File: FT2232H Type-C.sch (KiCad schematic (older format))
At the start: 34 parts, among them J1 CONN_01X20, J2 CONN_01X20, J3 USB_TYPE_C, U1 LD1117S33TR, U3 93CxxB, U4 FT2232H, Y1 12Mhz

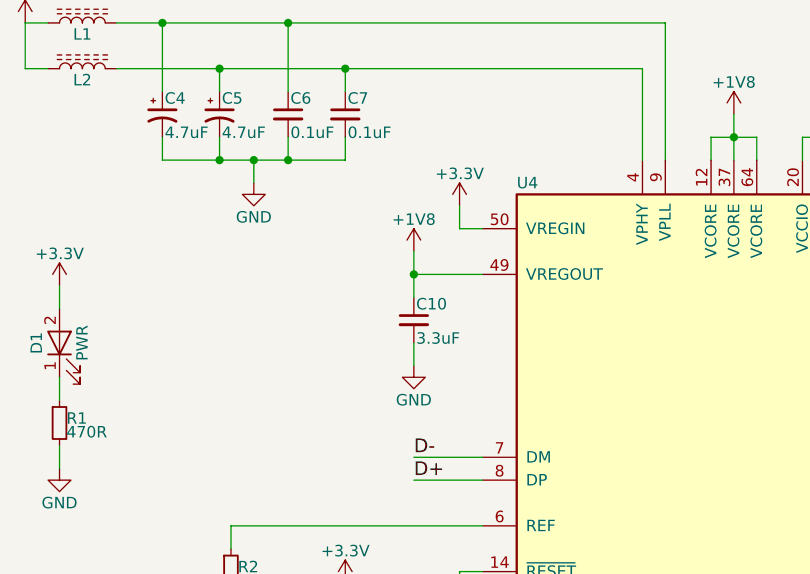
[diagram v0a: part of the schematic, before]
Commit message: Fix routing and add REGIN capacitor
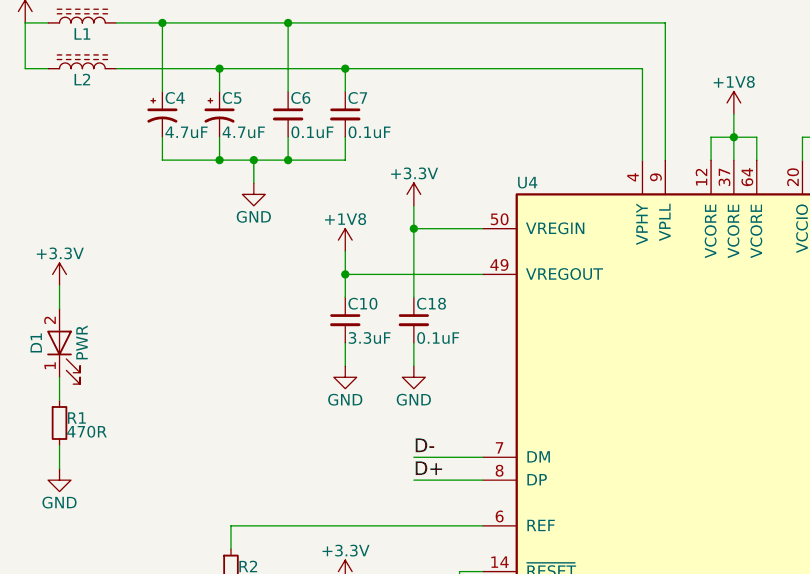
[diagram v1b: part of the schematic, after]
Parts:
- added C18: 0.1uF, Capacitors_SMD:C_0805_HandSoldering, symbol C_Small
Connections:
- net +3V3: now also C18.1
- net GND: now also C18.2
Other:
- moved on the sheet: C10
